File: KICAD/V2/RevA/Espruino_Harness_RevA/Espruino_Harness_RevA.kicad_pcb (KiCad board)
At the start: 2 copper layers, 183 parts, among them J1001 OPERATING_MODE, J201 EXTERNAL_ANALOG_STIMULUS_0_TO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, J302 MCP23017_GPIO, J401 MCP3008_ANALOGUE_BREAKOUT, J402 PIHUT_MICROSD_BREAKOUT_106696, J501 DS18B20_SENSOR_A, J502 DS18B20_SENSOR_B, J503 2K2_DQ_4K7, J504 DS2413_MODULE, J701 UART_PEER_DIAGNOSTIC, J902 PIXEL_SHIFTER_6066, Q1 2N7002, Q301 2N7002, Q302 2N7002, U1001 TPS2116DRL, U1002 TPS22917DBV, U301 MCP23017-E/SO, U401 MCP3008, U601 TMUX1511, U602 TMUX1511, U603 TMUX1511, U604 TMUX1511, U605 TMUX1511, U606 TMUX1511, U607 TPS3808G30DBVR, U608 TPS3808G30DBVR, U609 TPS3808G30DBVR, U610 MCP23017-E/SO RCTRL0, U611 MCP23017-E/SO RCTRL1, U701 TMUX1511

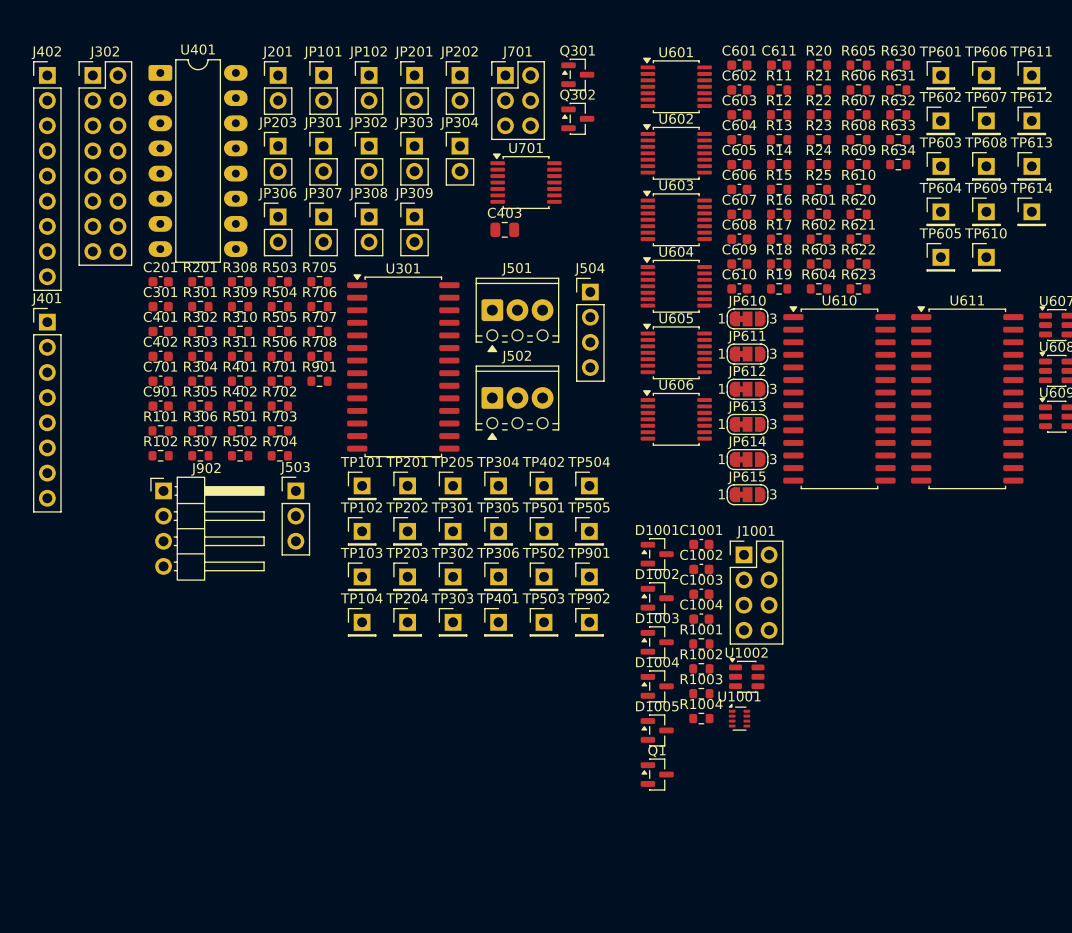
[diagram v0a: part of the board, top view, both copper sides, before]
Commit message: Add provisional Rev-A board outline
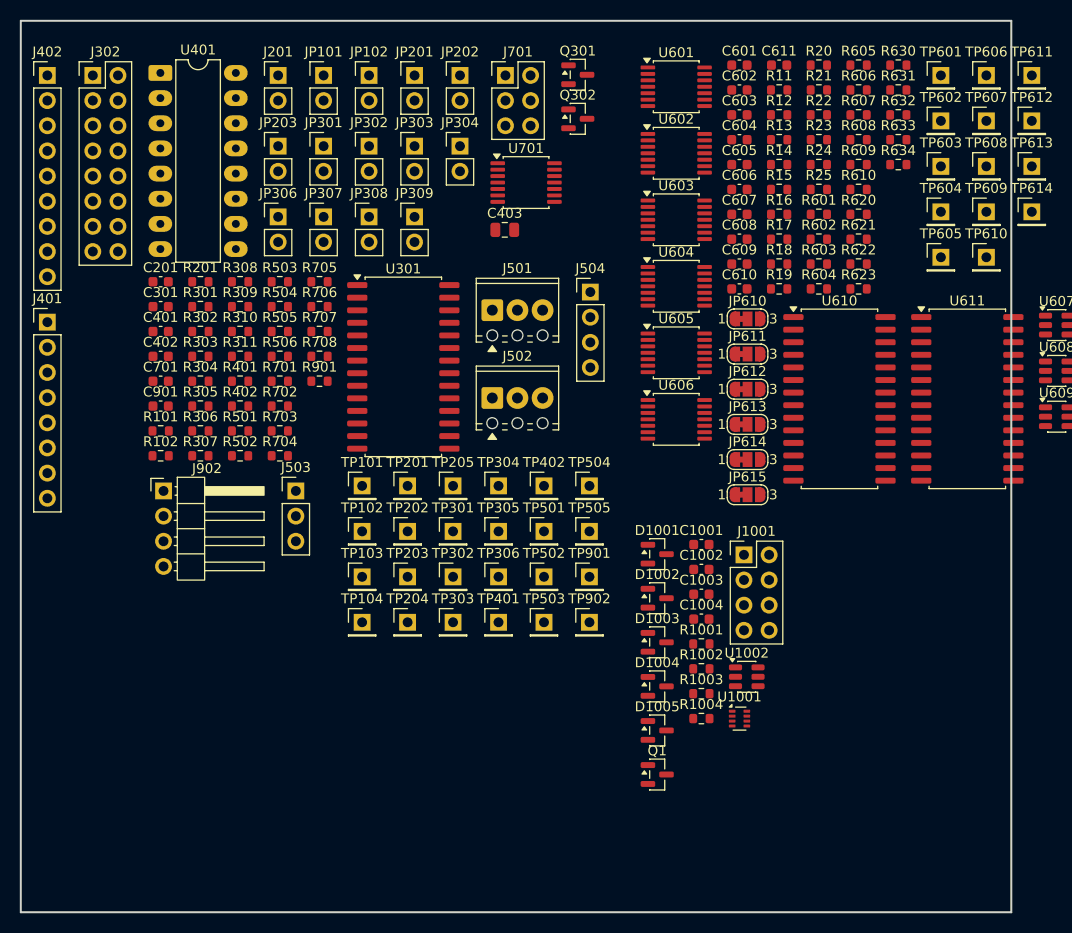
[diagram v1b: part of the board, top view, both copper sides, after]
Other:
- board outline added: 100 x 90 mm
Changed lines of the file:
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@@
 		)
+	)
+	(gr_rect
+		(start 84.18 50.72)
+		(end 184.18 140.72)
+		(stroke
+			(width 0.2)
+			(type solid)
+		)
+		(fill no)
+		(layer "Edge.Cuts")
 	)
 	(embedded_fonts no)

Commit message: Refresh provisional Rev-A PCB footprints
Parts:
- added C1005: 2.2 nF, Capacitor_SMD:C_0603_1608Metric, F.Cu at (25.3, 0.76)
- added C1101: 1uF, Capacitor_SMD:C_0603_1608Metric, F.Cu at (25.3, 3.27)
- added C1102: 100nF, Capacitor_SMD:C_0603_1608Metric, F.Cu at (25.3, 5.78)
- added C1103: 100nF, Capacitor_SMD:C_0603_1608Metric, F.Cu at (25.3, 8.29)
- added C1104: 100nF, Capacitor_SMD:C_0603_1608Metric, F.Cu at (25.3, 10.8)
- added C1105: 100nF, Capacitor_SMD:C_0603_1608Metric, F.Cu at (29.3, 0.76)
- added C1106: 100nF, Capacitor_SMD:C_0603_1608Metric, F.Cu at (29.3, 3.27)
- added C1107: 100nF, Capacitor_SMD:C_0603_1608Metric, F.Cu at (29.3, 5.78)
- added C1201: 100nF, Capacitor_SMD:C_0603_1608Metric, F.Cu at (1.50, 0.76)
- added JBP1: RACK_POWER_BACKPLANE, Connector_PinHeader_2.54mm:PinHeader_2x06_P2.54mm_Vertical, F.Cu at (25.6, 25.5)
- added Q1101: AO3401A, Package_TO_SOT_SMD:SOT-23, F.Cu at (38.3, 18.0)
- added Q1201: 2N7002, Package_TO_SOT_SMD:SOT-23, F.Cu at (18.9, 1.73)
- added Q1202: 2N7002, Package_TO_SOT_SMD:SOT-23, F.Cu at (18.9, 6.17)
- added R1009: 100k, Resistor_SMD:R_0603_1608Metric, F.Cu at (29.3, 8.29)
- added R1101: 0.050R 1.0%, Espruino_Harness_RevA:R_Shunt_Yageo_PE2512_CurrentSense, F.Cu at (47.4, 10.8)
- added R1102: 1.00R 1.0%, Espruino_Harness_RevA:R_Shunt_Bourns_CHP2512_CurrentSense, F.Cu at (48.3, 2.54)
- added R1103: 100k, Resistor_SMD:R_0603_1608Metric, F.Cu at (33.4, 3.27)
- added R1104: 100k, Resistor_SMD:R_0603_1608Metric, F.Cu at (33.4, 5.78)
- added R1105: 10k, Resistor_SMD:R_0603_1608Metric, F.Cu at (33.4, 8.29)
- added R1106: 100k, Resistor_SMD:R_0603_1608Metric, F.Cu at (33.4, 10.8)
- added R1107: 100k, Resistor_SMD:R_0603_1608Metric, F.Cu at (37.4, 0.76)
- added R1108: 10k, Resistor_SMD:R_0603_1608Metric, F.Cu at (37.4, 3.27)
- added R1110: 100k, Resistor_SMD:R_0603_1608Metric, F.Cu at (37.4, 5.78)
- added R1111: 66.5k 1%, Resistor_SMD:R_0603_1608Metric, F.Cu at (37.4, 8.29)
- added R1112: 10k, Resistor_SMD:R_0603_1608Metric, F.Cu at (37.4, 10.8)
- added R1201: 10k, Resistor_SMD:R_0603_1608Metric, F.Cu at (1.50, 3.27)
- added R1202: 10k, Resistor_SMD:R_0603_1608Metric, F.Cu at (1.50, 5.78)
- added R1203: 10k, Resistor_SMD:R_0603_1608Metric, F.Cu at (1.50, 8.29)
- added R1204: 100k, Resistor_SMD:R_0603_1608Metric, F.Cu at (1.50, 10.8)
- added R1205: 10k, Resistor_SMD:R_0603_1608Metric, F.Cu at (1.50, 13.3)
- added R1206: 100k, Resistor_SMD:R_0603_1608Metric, F.Cu at (1.50, 15.8)
- added R1207: 4.7k, Resistor_SMD:R_0603_1608Metric, F.Cu at (1.50, 18.3)
- added R1208: 4.7k, Resistor_SMD:R_0603_1608Metric, F.Cu at (1.50, 20.8)
- added U1101: TPS2559-Q1, Espruino_Harness_RevA:TPS2559Q1_DRC0010K_VSON10_EP, F.Cu at (100.2, 118.4)
- added U1102: TXU0101DBVR, Package_TO_SOT_SMD:SOT-23-6, F.Cu at (33.3, 18.2)
- added U1103: INA226, Package_SO:VSSOP-10_3x3mm_P0.5mm, F.Cu at (27.0, 14.3)
- added U1104: INA228, Package_SO:VSSOP-10_3x3mm_P0.5mm, F.Cu at (27.0, 18.9)
- added U1105: 74LVC2G08, Package_SO:VSSOP-8_2.3x2mm_P0.5mm, F.Cu at (33.5, 14.0)
- added U1201: MCP23017-E/SO, Package_SO:SOIC-28W_7.5x17.9mm_P1.27mm, F.Cu at (9.96, 9.35)
- D1001, D1002, D1003, D1004, D1005: value BAT54C -> BAT54C-E3-08
- J1001: value OPERATING_MODE -> OPERATING_MODE Selection
- Q1001: renamed from Q1; value 2N7002 -> DMN2024UQ-7
- moved Q1001 18.0 mm to (166.0, 130.5)
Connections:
- net /Power_Control/EXT_3V3 renamed /EXT_3V3
- net /Standard_Test_Blocks/TI_UART_B_RX renamed /TI_UART_B_RX
- net /Standard_Test_Blocks/TI_UART_B_TX renamed /TI_UART_B_TX
- C1001 pad 2: /Power_Control/TI_TARGET_3V3 -> /TI_TARGET_3V3
- C1003 pad 2: /Power_Control/ROUTING_LOGIC_3V3 -> /ROUTING_LOGIC_3V3
- C1004 pad 1: /Power_Control/TEST_BLOCK_3V3 -> /TEST_BLOCK_3V3
- D1003 pad 1: /Power_Control/TI_TARGET_3V3 -> /TI_TARGET_3V3
- D1005 pad 2: /Power_Control/TEST_BLOCK_POWER_EN -> /TEST_BLOCK_POWER_EN
- J1001 pad 5: /Power_Control/TI_TARGET_3V3 -> /TI_TARGET_3V3
- J402 pad 7: /Standard_Test_Blocks/TI_SPI_MISO -> /TI_SPI_MISO
- J501 pad 2: /Standard_Test_Blocks/TI_ONEWIRE_DQ -> /TI_ONEWIRE_DQ
- J502 pad 2: /Standard_Test_Blocks/TI_ONEWIRE_DQ -> /TI_ONEWIRE_DQ
- J503 pad 2: /Standard_Test_Blocks/TI_ONEWIRE_DQ -> /TI_ONEWIRE_DQ
- J504 pad 3: /Standard_Test_Blocks/TI_ONEWIRE_DQ -> /TI_ONEWIRE_DQ
- JP101 pad 2: /Standard_Test_Blocks/TI_GPIO_LOOP_A_IN -> /TI_GPIO_LOOP_A_IN
- JP102 pad 2: /Standard_Test_Blocks/TI_GPIO_LOOP_B_IN -> /TI_GPIO_LOOP_B_IN
- JP201 pad 1: /Standard_Test_Blocks/TI_ANALOG_PWM_OUT -> /TI_ANALOG_PWM_OUT
- JP202 pad 2: /Standard_Test_Blocks/TI_ANALOG_ADC_IN -> /TI_ANALOG_ADC_IN
- Q302 pad 3: /Standard_Test_Blocks/SUP_EVENT_IN -> /SUP_EVENT_IN
- R101 pad 1: /Standard_Test_Blocks/TI_GPIO_LOOP_A_OUT -> /TI_GPIO_LOOP_A_OUT
- R102 pad 1: /Standard_Test_Blocks/TI_GPIO_LOOP_B_OUT -> /TI_GPIO_LOOP_B_OUT
- R505 pad 2: /Standard_Test_Blocks/TI_ONEWIRE_GPIO_A_FB -> /TI_ONEWIRE_GPIO_A_FB
- R506 pad 2: /Standard_Test_Blocks/TI_ONEWIRE_GPIO_B_FB -> /TI_ONEWIRE_GPIO_B_FB
- R702 pad 2: /Standard_Test_Blocks/TI_UART_A_RX -> /TI_UART_A_RX
- R704 pad 2: /Standard_Test_Blocks/TI_UART_A_RX -> /TI_UART_A_RX
- R901 pad 1: /Standard_Test_Blocks/TI_RGB_DATA -> /TI_RGB_DATA
- TP101 pad 1: /Standard_Test_Blocks/TI_GPIO_LOOP_A_OUT -> /TI_GPIO_LOOP_A_OUT
- TP102 pad 1: /Standard_Test_Blocks/TI_GPIO_LOOP_A_IN -> /TI_GPIO_LOOP_A_IN
- TP103 pad 1: /Standard_Test_Blocks/TI_GPIO_LOOP_B_OUT -> /TI_GPIO_LOOP_B_OUT
- TP104 pad 1: /Standard_Test_Blocks/TI_GPIO_LOOP_B_IN -> /TI_GPIO_LOOP_B_IN
- TP201 pad 1: /Standard_Test_Blocks/TI_ANALOG_PWM_OUT -> /TI_ANALOG_PWM_OUT
- TP203 pad 1: /Standard_Test_Blocks/TI_ANALOG_ADC_IN -> /TI_ANALOG_ADC_IN
- TP501 pad 1: /Standard_Test_Blocks/TI_ONEWIRE_DQ -> /TI_ONEWIRE_DQ
- U1001 pad 2: /Power_Control/ROUTING_LOGIC_3V3 -> /ROUTING_LOGIC_3V3
- U1001 pad 3: /Power_Control/TI_TARGET_3V3 -> /TI_TARGET_3V3
- U1001 pad 7: /Power_Control/ROUTING_LOGIC_3V3 -> /ROUTING_LOGIC_3V3
- U1002 pad 1: /Power_Control/ROUTING_LOGIC_3V3 -> /ROUTING_LOGIC_3V3
- U1002 pad 4: unconnected-(U1002-CT-Pad4) -> Net-(U1002-CT)
- U1002 pad 5: /Power_Control/TEST_BLOCK_3V3 -> /TEST_BLOCK_3V3
- U1002 pad 6: /Power_Control/TEST_BLOCK_3V3 -> /TEST_BLOCK_3V3
- U401 pad 12: /Standard_Test_Blocks/TI_SPI_MISO -> /TI_SPI_MISO
- U701 pad 2: /Standard_Test_Blocks/TI_UART_A_TX -> /TI_UART_A_TX
- U701 pad 9: /Standard_Test_Blocks/TI_UART_A_TX -> /TI_UART_A_TX

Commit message: Implement RC01 routing baseline metadata
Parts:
- removed R13, R18, R23, R25, R603, R608: 100k, Resistor_SMD:R_0603_1608Metric

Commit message: Verify RC02 routing control baseline
Add the qualified fixed-I2C isolation and Hardware Clear implementation, exact component metadata, deterministic RC02 connectivity contract, accepted ERC/connectivity evidence, and visual review records. Synchronize the draft PCB and document the PCB-stage workflow while preserving the verified RC01 baseline.
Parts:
- added C621: 4.7nF, Capacitor_SMD:C_0603_1608Metric, F.Cu at (174.5, 116.9)
- added C622: 4.7nF, Capacitor_SMD:C_0603_1608Metric, F.Cu at (174.5, 119.4)
- added C623: 4.7nF, Capacitor_SMD:C_0603_1608Metric, F.Cu at (174.5, 121.9)
- added Q1203: DMG2302UKQ-7, Package_TO_SOT_SMD:SOT-23, F.Cu at (178.9, 110.8)
- added R1209: 10k, Resistor_SMD:R_0603_1608Metric, F.Cu at (174.5, 109.9)
- added R1210: 100k, Resistor_SMD:R_0603_1608Metric, F.Cu at (174.5, 112.4)
- JP613: value A0 default 1 -> A0 default 0
- JP614: value A1 default 0 -> A1 default 1
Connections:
- U1201 pad 27: unconnected-(U1201-GPA6-Pad27) -> /V2 Rev-A Rack Control Endpoint/ROUTE_CLEAR_REQUEST

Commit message: Verify TB01 digital GPIO loopback baseline
Accept the two independent 470 ohm protected loopback paths using retained V1 functional evidence and Rev-A SMD component/package review.

Add the project-local isolation-header symbol, exact resistor/header/shunt metadata, focused visual evidence, deterministic TB01 contract, clean hierarchy ERC, synchronized PCB metadata and recorded downstream layout checks.
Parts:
- moved JP102 69.4 mm to (115.3, 125.5)
- moved R102 36.6 mm to (119.6, 124.5)

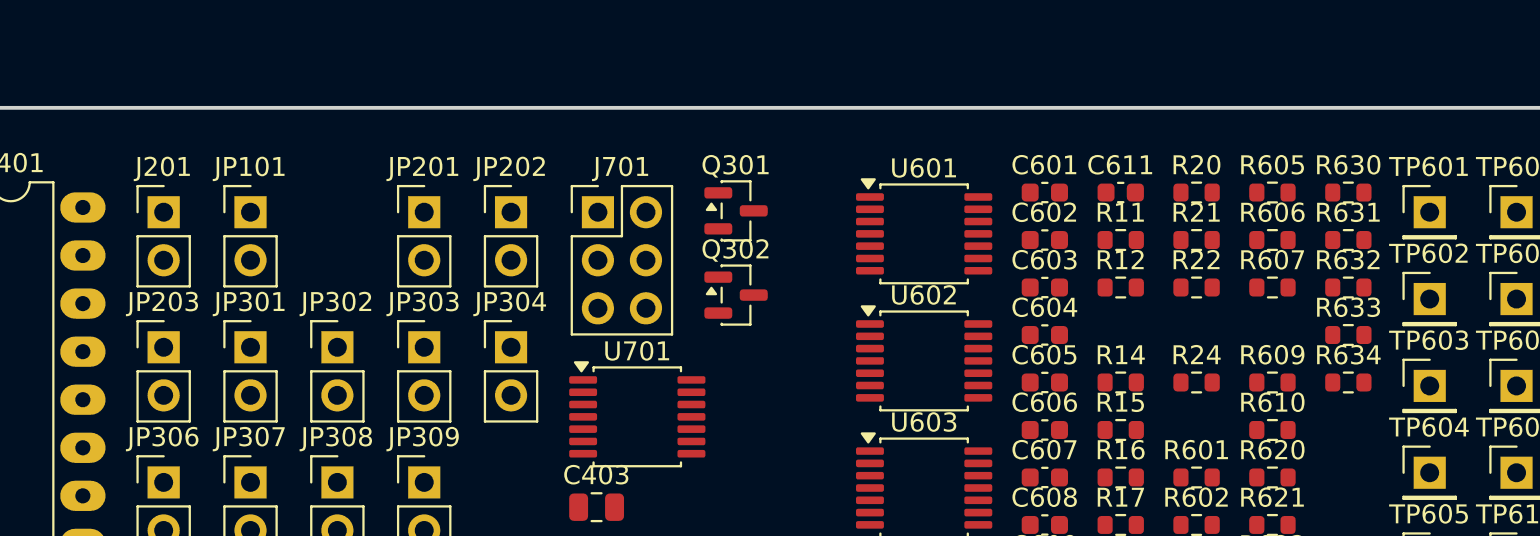
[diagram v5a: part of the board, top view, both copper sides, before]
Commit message: Verify TB02 analogue PWM feedback baseline
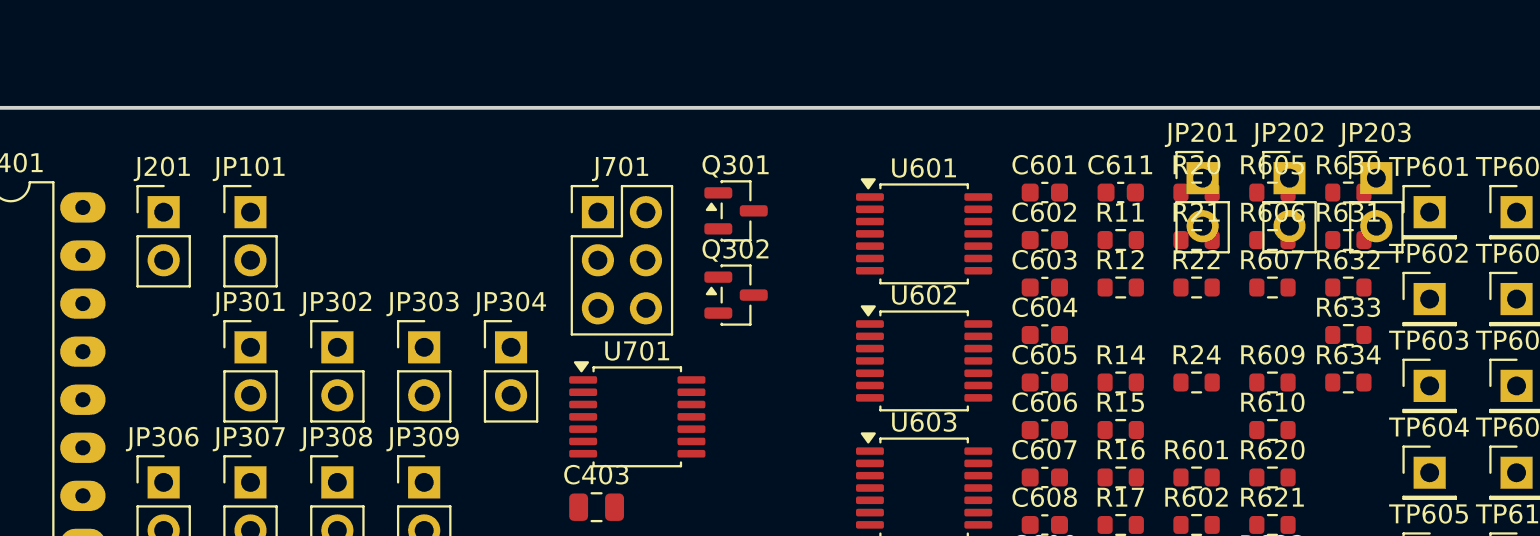
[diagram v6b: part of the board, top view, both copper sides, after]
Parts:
- moved JP203 64.7 mm to (174.2, 54.4)
- moved JP201 41.2 mm to (165.1, 54.4)
- moved JP202 41.2 mm to (169.7, 54.4)
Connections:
- J401 pad 1: /Standard_Test_Blocks/ANALOG_FB -> /Standard_Test_Blocks/MCP3008_CH0
- U401 pad 1: /Standard_Test_Blocks/ANALOG_FB -> /Standard_Test_Blocks/MCP3008_CH0
